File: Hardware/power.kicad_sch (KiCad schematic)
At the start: 20 parts, among them U3 LM66200DRLR, U4 MAX77827AEFD+T, U5 SC4215ASTRT

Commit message: PCB mid design
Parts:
- C23: footprint Capacitor_SMD:C_0603_1608Metric -> Capacitor_SMD:C_0805_2012Metric
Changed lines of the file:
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@@
 			)
 		)
-		(property "Footprint" "Capacitor_SMD:C_0603_1608Metric"
+		(property "Footprint" "Capacitor_SMD:C_0805_2012Metric"
 			(at 179.07 54.61 0)
 			(effects

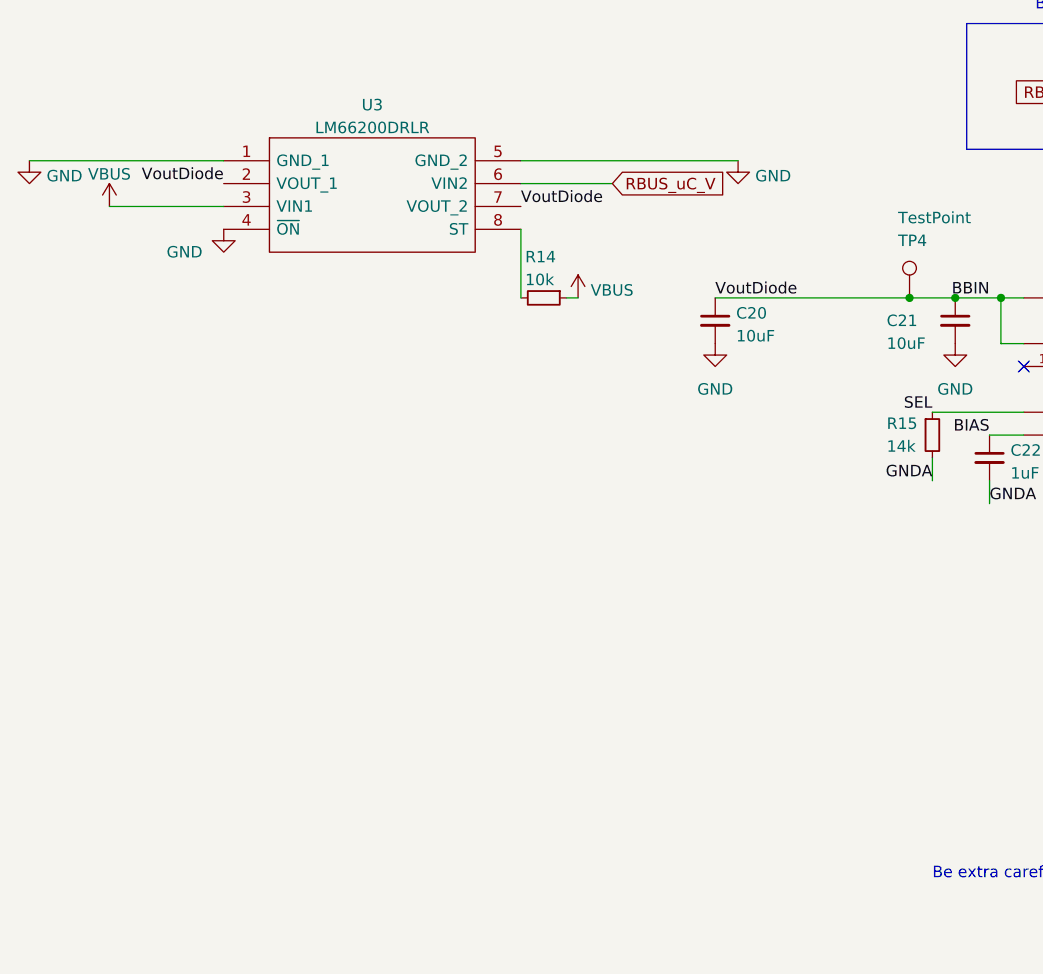
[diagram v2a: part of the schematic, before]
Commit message: Swapped battery & nichrome positions
fixed crystal and other small things
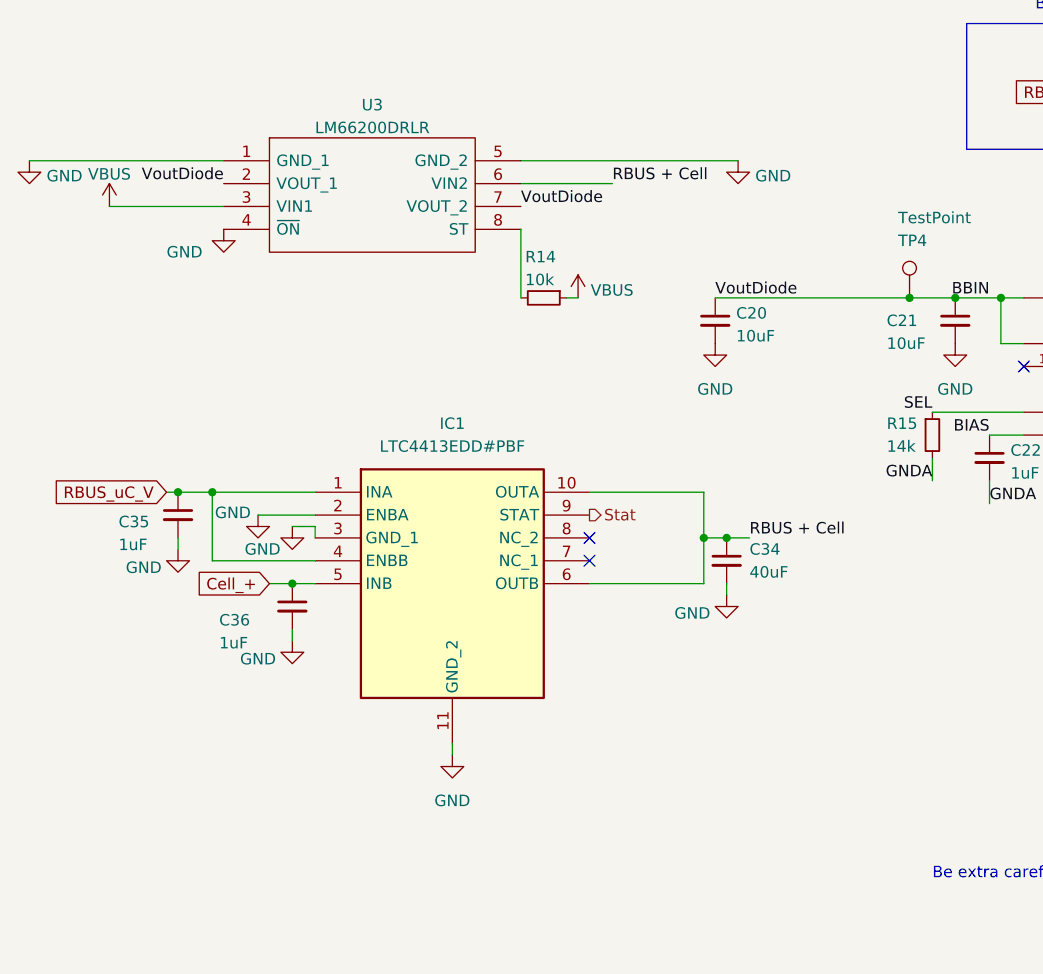
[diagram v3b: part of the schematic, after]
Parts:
- added C34: 40uF, Capacitor_SMD:C_0402_1005Metric, symbol Device:C_Small
- added C35, C36: 1uF, Capacitor_SMD:C_0402_1005Metric, symbol Device:C_Small
- added IC1: LTC4413EDD#PBF, iclr:SON50P300X300X80-11N-D, symbol iclr:LTC4413EDD#PBF
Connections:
- net GND: now also C34.2, C35.2, C36.2, IC1.11 (GND_2), IC1.2 (ENBA), IC1.3 (GND_1)
- net RBUS_uC_V: now also C35.1, IC1.1 (INA), IC1.4 (ENBB); no longer U3.6 (VIN2)
- new net Cell_+: C36.1, IC1.5 (INB)
- new net RBUS + Cell: C34.1, IC1.10 (OUTA), IC1.6 (OUTB), U3.6 (VIN2)
- new net Stat: IC1.9 (STAT)
- no-connect marks 4 -> 6

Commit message: Applied more review suggestions
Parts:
- C23: footprint Capacitor_SMD:C_0805_2012Metric -> Capacitor_SMD:C_0603_1608Metric
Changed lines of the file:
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@@
 			)
 		)
-		(property "Footprint" "Capacitor_SMD:C_0805_2012Metric"
+		(property "Footprint" "Capacitor_SMD:C_0603_1608Metric"
 			(at 179.07 54.61 0)
 			(effects

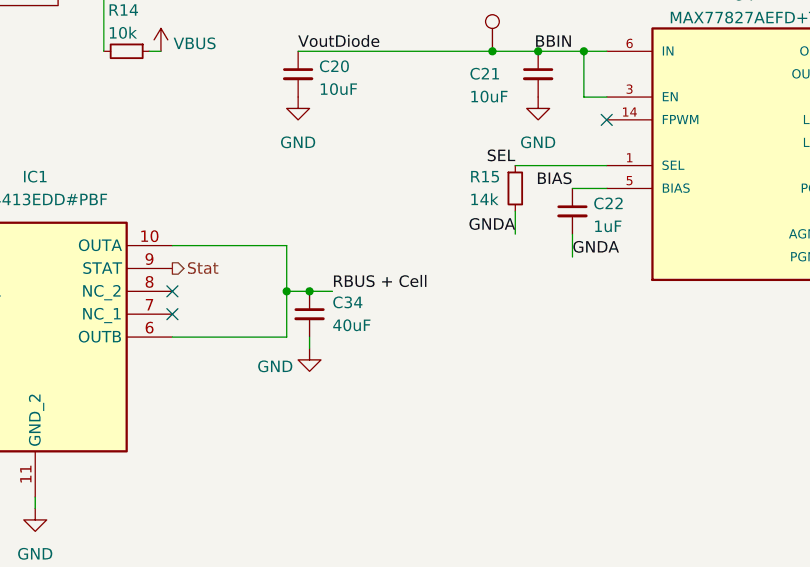
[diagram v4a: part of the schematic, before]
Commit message: Testpoints + footprints + AGND plane
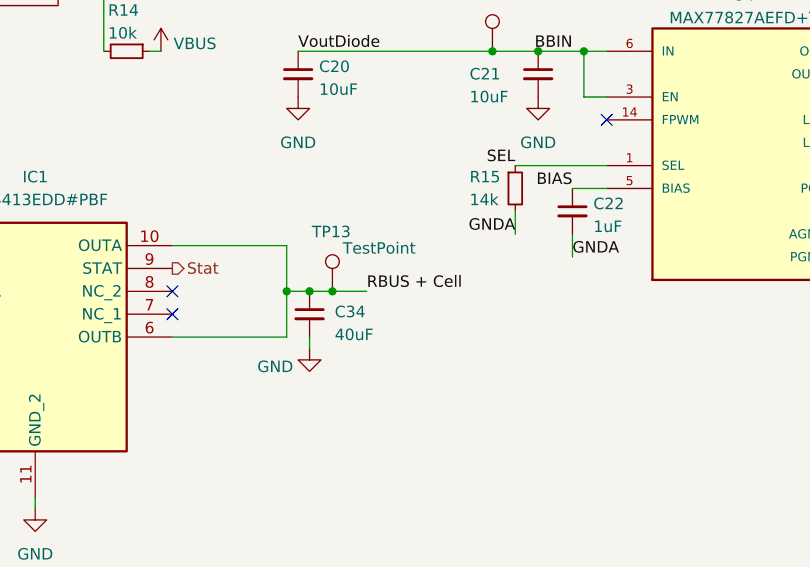
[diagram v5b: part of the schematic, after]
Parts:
- added TP13: TestPoint, TestPoint:TestPoint_Pad_D1.0mm, symbol Connector:TestPoint
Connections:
- net RBUS + Cell: now also TP13.1
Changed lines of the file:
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@@
+	)
+	(junction
+		(at 105.41 78.74)
+		(diameter 0)
+		(color 0 0 0 0)
 	)
 	(junction
@@
 	(wire
 		(pts
+			(xy 109.22 78.74) (xy 105.41 78.74)
+		)
+		(stroke
+			(width 0)
+			(type default)
+		)
+	)
+	(wire
+		(pts
 			(xy 171.45 64.77) (xy 166.37 64.77)
 		)
@@
 	(wire
 		(pts
+			(xy 54.61 88.9) (xy 54.61 90.17)
+		)
+		(stroke
+			(width 0)
+			(type default)
+		)
+	)
+	(wire
+		(pts
+			(xy 54.61 77.47) (xy 57.15 77.47)
+		)
+		(stroke
+			(width 0)
+			(type default)
+		)
+	)
+	(wire
+		(pts
+			(xy 153.67 119.38) (xy 158.75 119.38)
+		)
+		(stroke
+			(width 0)
+			(type default)
+		)
+	)
+	(wire
+		(pts
 			(xy 105.41 78.74) (xy 102.87 78.74)
-		)
-		(stroke
-			(width 0)
-			(type default)
-		)
-	)
-	(wire
-		(pts
-			(xy 54.61 88.9) (xy 54.61 90.17)
-		)
-		(stroke
-			(width 0)
-			(type default)
-		)
-	)
-	(wire
-		(pts
-			(xy 54.61 77.47) (xy 57.15 77.47)
-		)
-		(stroke
-			(width 0)
-			(type default)
-		)
-	)
-	(wire
-		(pts
-			(xy 153.67 119.38) (xy 158.75 119.38)
 		)
 		(stroke
@@
 	)
 	(label "RBUS + Cell"
-		(at 105.41 78.74 0)
+		(at 109.22 78.74 0)
 		(effects
 			(font
@@
 	)
 	(symbol
+		(lib_id "Connector:TestPoint")
+		(at 105.41 78.74 0)
+		(unit 1)
+		(exclude_from_sim no)
+		(in_bom yes)
+		(on_board yes)
+		(dnp no)
+		(property "Reference" "TP13"
+			(at 103.124 72.136 0)
+			(effects
+				(font
+					(size 1.27 1.27)
+				)
+				(justify left)
+			)
+		)
+		(property "Value" "TestPoint"
+			(at 106.553 73.9648 0)
+			(effects
+				(font
+					(size 1.27 1.27)
+				)
+				(justify left)
+			)
+		)
+		(property "Footprint" "TestPoint:TestPoint_Pad_D1.0mm"
+			(at 110.49 78.74 0)
+			(effects
+				(font
+					(size 1.27 1.27)
+				)
+				(hide yes)
+			)
+		)
+		(property "Datasheet" "~"
+			(at 110.49 78.74 0)
+			(effects
+				(font
+					(size 1.27 1.27)
+				)
+				(hide yes)
+			)
+		)
+		(property "Description" ""
+			(at 105.41 78.74 0)
+			(effects
+				(font
+					(size 1.27 1.27)
+				)
+				(hide yes)
+			)
+		)
+		(pin "1"
+		)
+		(instances
+			(project "Main board"
+				(path "/7db990e4-92e1-4f99-b4d2-435bbec1ba83/48a413b4-b7c2-44ac-971c-583c31b73475"
+					(reference "TP13")
+					(unit 1)
+				)
+			)
+		)
+	)
+	(symbol
 		(lib_id "Device:R_Small")
 		(at 240.03 64.77 0)
@@
 		(on_board yes)
 		(dnp no)
-		(fields_autoplaced yes)
 		(property "Reference" "C34"
-			(at 105.41 80.0162 0)
+			(at 105.664 81.026 0)
 			(effects
 				(font
@@
 		)
 		(property "Value" "40uF"
-			(at 105.41 82.5562 0)
-			(effects
-				(font
+			(at 105.664 83.566 0)
+			(effects
+				(font

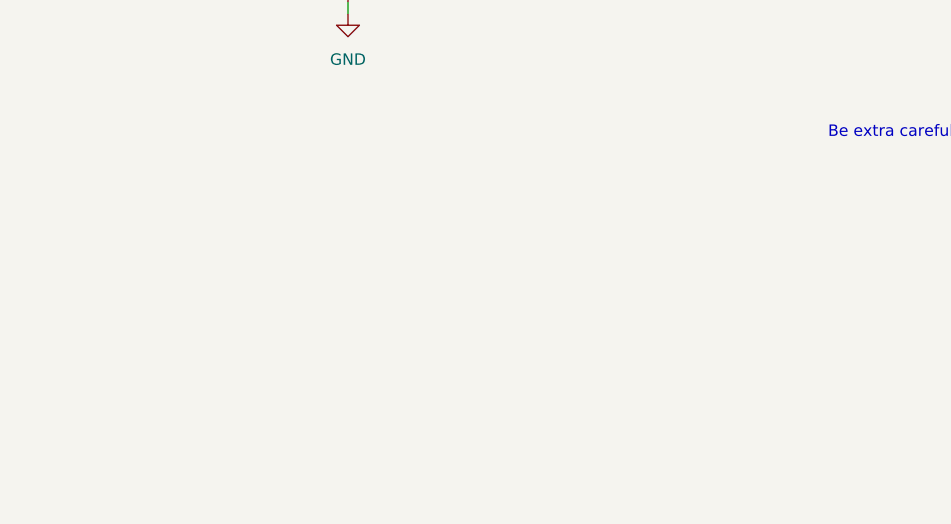
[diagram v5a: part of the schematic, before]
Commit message: Added MOSFET circuit to turn cell power on/off
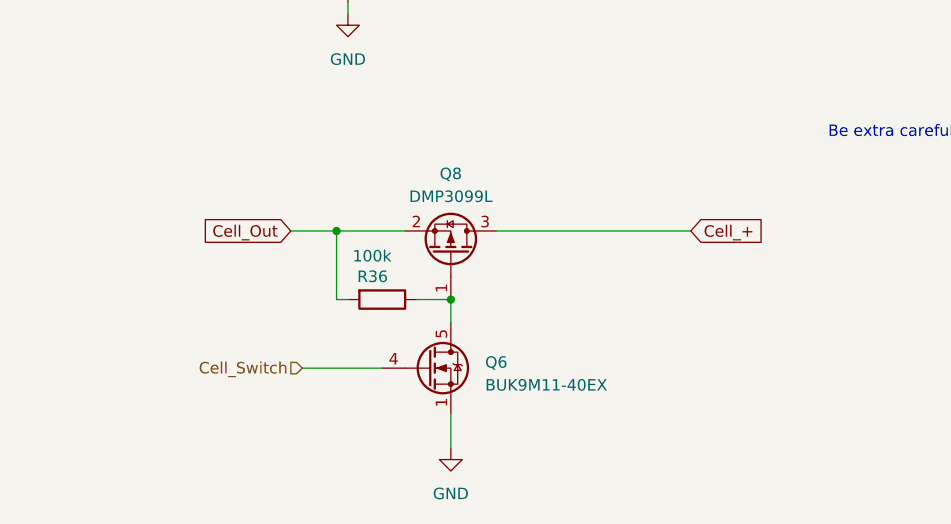
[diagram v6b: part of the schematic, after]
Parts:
- added Q6: BUK9M11-40EX, Package_TO_SOT_SMD:LFPAK33, symbol Transistor_FET:BUK9M11-40EX
- added Q8: DMP3099L, Package_TO_SOT_SMD:SOT-23, symbol Transistor_FET:DMP3099L
- added R36: 100k, Resistor_SMD:R_0402_1005Metric, symbol Device:R
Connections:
- net Cell_+: now also Q8.3 (D)
- net GND: now also Q6.1 (S), Q6.2 (S), Q6.3 (S)
- new net: Q6.5 (D), Q8.1 (G), R36.1
- new net Cell_Out: Q8.2 (S), R36.2
- new net Cell_Switch: Q6.4 (G)

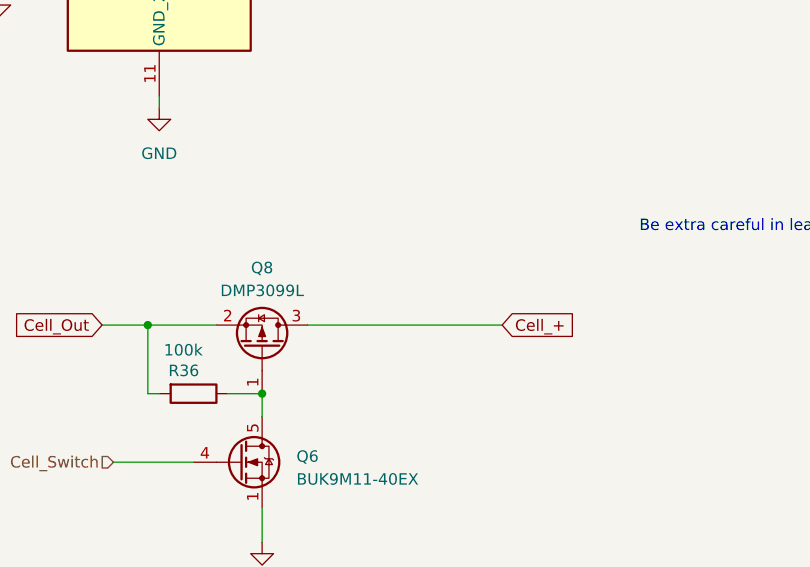
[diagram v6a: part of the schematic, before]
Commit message: Test point + Net shape change
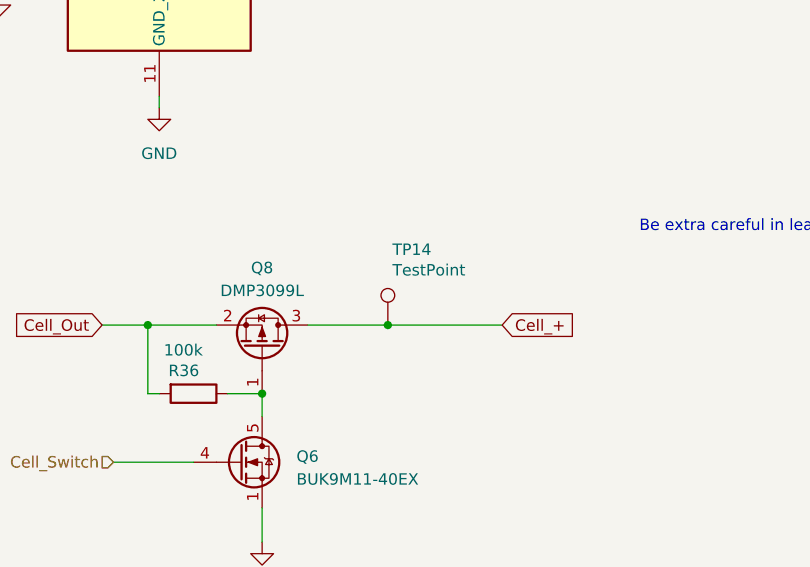
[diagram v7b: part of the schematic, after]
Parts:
- added TP14: TestPoint, TestPoint:TestPoint_Pad_D1.5mm, symbol Connector:TestPoint
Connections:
- net Cell_+: now also TP14.1
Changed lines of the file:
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@@
+	)
+	(junction
+		(at 97.79 127)
+		(diameter 0)
+		(color 0 0 0 0)
 	)
 	(junction
@@
 	(wire
 		(pts
+			(xy 97.79 127) (xy 110.49 127)
+		)
+		(stroke
+			(width 0)
+			(type default)
+		)
+	)
+	(wire
+		(pts
 			(xy 252.73 57.15) (xy 255.27 57.15)
 		)
@@
 	(wire
 		(pts
-			(xy 88.9 127) (xy 110.49 127)
+			(xy 88.9 127) (xy 97.79 127)
 		)
 		(stroke
@@
 					(unit 1)
 				)
+			)
+		)
+	)
+	(symbol
+		(lib_id "Connector:TestPoint")
+		(at 97.79 127 0)
+		(unit 1)
+		(exclude_from_sim no)
+		(in_bom yes)
+		(on_board yes)
+		(dnp no)
+		(property "Reference" "TP14"
+			(at 98.298 118.618 0)
+			(effects
+				(font
+					(size 1.27 1.27)
+				)
+				(justify left)
+			)
+		)
+		(property "Value" "TestPoint"
+			(at 98.298 120.904 0)
+			(effects
+				(font
+					(size 1.27 1.27)
+				)
+				(justify left)
+			)
+		)
+		(property "Footprint" "TestPoint:TestPoint_Pad_D1.5mm"
+			(at 102.87 127 0)
+			(effects
+				(font
+					(size 1.27 1.27)
+				)
+				(hide yes)
+			)
+		)
+		(property "Datasheet" "~"
+			(at 102.87 127 0)
+			(effects
+				(font
+					(size 1.27 1.27)
+				)
+				(hide yes)
+			)
+		)
+		(property "Description" ""
+			(at 97.79 127 0)
+			(effects
+				(font
+					(size 1.27 1.27)
+				)
+				(hide yes)
+			)
+		)
+		(pin "1"
+		)
+		(instances
+			(project "Main board"
+				(path "/7db990e4-92e1-4f99-b4d2-435bbec1ba83/48a413b4-b7c2-44ac-971c-583c31b73475"
+					(reference "TP14")
+					(unit 1)
+				)
